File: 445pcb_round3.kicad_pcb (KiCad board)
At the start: 2 copper layers, 40 parts, among them J1 LED, J10 AVR-ISP-6, J2 LED, J3 LED, J4 SG3, J5 SG4, J6 SG5, J7 SG6, J8 SG1, J9 SG2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

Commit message: Add files via upload
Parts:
- added J11: SG1, Connector_Molex:Molex_KK-254_AE-6410-02A_1x02_P2.54mm_Vertical, F.Cu at (81.3, 76.2)
- added J13: LED, Connector_Molex:Molex_KK-254_AE-6410-02A_1x02_P2.54mm_Vertical, F.Cu at (81.3, 68.6)
- added P1: USB_C_Plug_USB2.0, Connector_USB:USB_C_Plug_Molex_105444, F.Cu at (78.7, 58.7)
- added R25: 1k, Resistor_SMD:R_0805_2012Metric_Pad1.20x1.40mm_HandSolder, F.Cu at (90.4, 73.7)
- added SW1: SW_SPST, Button_Switch_THT:SW_DIP_SPSTx01_Slide_9.78x4.72mm_W7.62mm_P2.54mm, F.Cu at (90.2, 80.5)
- moved R11 9.16 mm to (138.2, 61.0)
- moved R19 8.89 mm to (86.4, 48.3), turned to 90 degrees
- turned R8 to 180 degrees
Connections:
- R3 pad 1: Net-(U3-PD0) -> Net-(U3-PD3)
- U3 pad 1: unconnected-(U3-PD3-Pad1) -> Net-(U3-PD3)
- U3 pad 30: Net-(U3-PD0) -> UART RXD
- U3 pad 31: unconnected-(U3-PD1-Pad31) -> UART TXD
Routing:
- net Net-(U3-PD3): track 0.00 -> 134.4 mm, vias 0 -> 2
- net Net-(U3-PD0): track 118.4 -> 0.00 mm
- net Vdiff1: track 19.0 -> 98.8 mm, vias 0 -> 2
- net GND: track 360.4 -> 431.7 mm, vias 0 -> 2
- net +5V: track 269.5 -> 322.4 mm, vias 0 -> 5
- net Net-(U1-REGOUT): track 0.00 -> 24.3 mm, vias 0 -> 1
- net UART RXD: track 0.00 -> 21.3 mm, vias 0 -> 1
- net UART TXD: track 0.00 -> 19.9 mm, vias 0 -> 1
- net Net-(J11-Pin_2): track 0.00 -> 17.9 mm
- net MCU_DL: track 0.00 -> 17.0 mm, vias 0 -> 2
- net Net-(U5A--): track 13.2 -> 28.6 mm, vias 0 -> 2
- net unconnected-(P1-SHIELD-PadS1): track 0.00 -> 14.2 mm, vias 0 -> 1
- net Net-(J11-Pin_1): track 0.00 -> 10.7 mm
- net Net-(U4A-+): track 7.84 -> 15.8 mm, vias 0 -> 1
- net RST: track 32.0 -> 24.3 mm
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
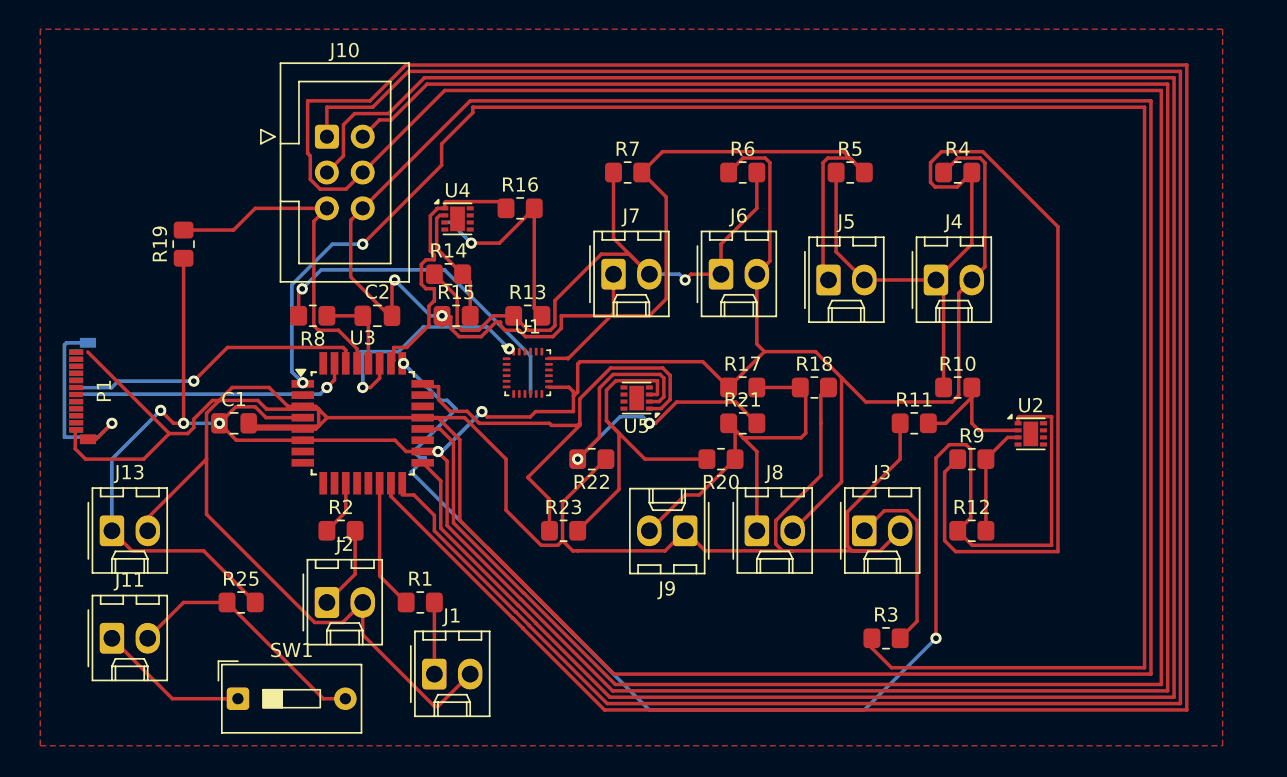
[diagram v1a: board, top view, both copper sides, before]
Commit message: adding power to op-amps, switching USB to connector, zener diode
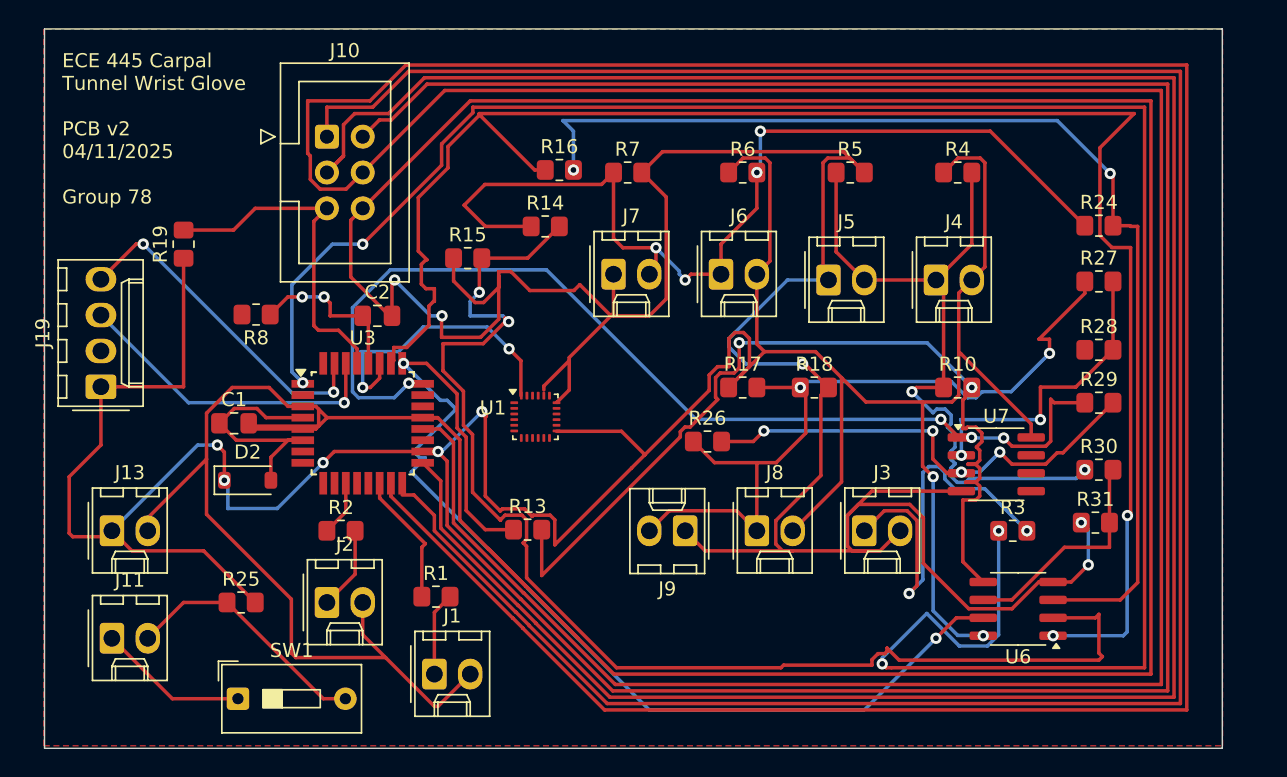
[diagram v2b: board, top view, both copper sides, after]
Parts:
- removed P1: USB_C_Plug_USB2.0, Connector_USB:USB_C_Plug_Molex_105444
- removed R11, R12, R22, R23: 3.3M, Resistor_SMD:R_0805_2012Metric_Pad1.20x1.40mm_HandSolder
- removed R20, R21, R9: 10k, Resistor_SMD:R_0805_2012Metric_Pad1.20x1.40mm_HandSolder
- removed U2, U4, U5: LM358_DFN, Package_DFN_QFN:DFN-8-1EP_2x2mm_P0.5mm_EP1.05x1.75mm
- added D2: MBR0520, Diode_SMD:D_SOD-123, F.Cu at (90.9, 65.0)
- added J19: Conn_01x04_Pin, Connector_Molex:Molex_KK-254_AE-6410-04A_1x04_P2.54mm_Vertical, F.Cu at (80.5, 58.4)
- added R24: 10k, Resistor_SMD:R_0805_2012Metric_Pad1.20x1.40mm_HandSolder, F.Cu at (151.2, 47.0)
- added R26: 10k, Resistor_SMD:R_0805_2012Metric_Pad1.20x1.40mm_HandSolder, F.Cu at (123.5, 62.2)
- added R27: 10k, Resistor_SMD:R_0805_2012Metric_Pad1.20x1.40mm_HandSolder, F.Cu at (151.2, 50.9)
- added R28: 3.3M, Resistor_SMD:R_0805_2012Metric_Pad1.20x1.40mm_HandSolder, F.Cu at (151.2, 55.8)
- added R29: 3.3M, Resistor_SMD:R_0805_2012Metric_Pad1.20x1.40mm_HandSolder, F.Cu at (151.2, 59.5)
- added R30: 10k, Resistor_SMD:R_0805_2012Metric_Pad1.20x1.40mm_HandSolder, F.Cu at (151.2, 64.2)
- added R31: 3.3M, Resistor_SMD:R_0805_2012Metric_Pad1.20x1.40mm_HandSolder, F.Cu at (151.0, 68.0)
- added U6: LM358DT, Package_SO:SOIC-8_3.9x4.9mm_P1.27mm, F.Cu at (145.5, 74.1)
- added U7: LM358DT, Package_SO:SOIC-8_3.9x4.9mm_P1.27mm, F.Cu at (144.0, 63.9)
- R13: value 10k -> 3.3M
- moved R13 15.2 mm to (110.8, 68.5)
- moved R3 11.8 mm to (145.1, 68.6)
- moved R14 7.65 mm to (112.0, 47.0)
- moved R15 4.17 mm to (106.5, 49.2)
- moved R8 4.02 mm to (91.5, 53.2)
- moved R16 3.89 mm to (113.0, 43.0)
- moved U1 3.17 mm to (111.3, 60.5)
- moved R1 1.18 mm to (104.2, 73.2)
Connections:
- C1 pad 1: +5V -> Net-(D2-A)
- R10 pad 2: Net-(U2A--) -> Net-(U6-IN2+)
- R13 pad 1: V2+ -> Vdiff1
- R13 pad 2: Net-(U4A-+) -> Net-(U6-IN2+)
- R16 pad 2: Net-(U4A-+) -> Net-(U6-IN1+)
- U1 pad 9: unconnected-(U1-SDO/AD0-Pad9) -> GND
- U3 pad 4: +5V -> Net-(D2-A)
- U3 pad 6: +5V -> Net-(D2-A)
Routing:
- net Vdiff2: track 20.1 -> 120.2 mm, vias 0 -> 2
- net Net-(U6-IN1-): track 8.55 -> 91.4 mm, vias 0 -> 2
- net Net-(U6-IN1+): track 0.00 -> 81.5 mm, vias 0 -> 2
- net Net-(U6-IN2+): track 0.00 -> 64.5 mm, vias 0 -> 2
- net +5V: track 322.4 -> 384.5 mm, vias 5 -> 7
- net Vdiff: track 35.5 -> 71.3 mm, vias 0 -> 4
- net Net-(U7-IN1+): track 0.00 -> 33.2 mm, vias 0 -> 4
- net V1+: track 84.0 -> 51.1 mm, vias 0 -> 2
- net Net-(U5A--): track 28.6 -> 0.00 mm, vias 2 -> 0
- net V+: track 30.9 -> 56.4 mm, vias 0 -> 2
- net Net-(U5A-+): track 25.2 -> 0.00 mm
- net V2+: track 44.7 -> 69.9 mm, vias 2 -> 4
- net Net-(U1-REGOUT): track 24.3 -> 0.00 mm, vias 1 -> 0
- net Net-(U7-IN1-): track 0.00 -> 21.6 mm, vias 0 -> 2
- net Vdiff1: track 98.8 -> 79.1 mm
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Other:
- board outline added: 83.5 x 51 mm
- board text added: "ECE 445 Carpal Tunnel Wrist Glove PCB v2 04/11/2025 Group 78"

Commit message: Add files via upload
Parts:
- moved U7 25.7 mm to (119.3, 71.1)
- moved U6 16.2 mm to (129.6, 71.1)
- moved R30 14.1 mm to (137.5, 67.3)
- moved SW1 13.8 mm to (103.5, 76.8)
- moved R31 13.8 mm to (137.4, 70.5)
- moved R24 12.9 mm to (139.4, 52.1)
- moved R27 12.8 mm to (139.4, 55.9)
- moved R29 12.5 mm to (139.4, 63.5)
- moved R28 12.5 mm to (139.4, 59.7)
- moved R17 10.3 mm to (115.8, 56.5)
- moved R10 10.2 mm to (131.2, 56.5)
- moved R3 8.90 mm to (137.4, 73.0)
- moved R4 8.16 mm to (133.1, 43.2)
- moved J2 8.04 mm to (88.9, 76.2)
- moved J1 8.03 mm to (96.5, 76.2)
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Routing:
- net MOSI: track 347.2 -> 150.8 mm, vias 0 -> 1
- net GND: track 434.7 -> 246.0 mm, vias 5 -> 9
- net +5V: track 384.5 -> 300.1 mm, vias 7 -> 8
- net Net-(J11-Pin_2): track 17.9 -> 60.0 mm
- net Vdiff1: track 79.1 -> 42.0 mm, vias 2 -> 3
- net Net-(U3-PD3): track 151.1 -> 118.6 mm, vias 4 -> 2
- net Net-(U6-IN2+): track 64.5 -> 33.0 mm, vias 2 -> 0
- net Net-(U6-IN1+): track 81.5 -> 111.6 mm, vias 2 -> 3
- net Net-(U6-IN1-): track 91.4 -> 63.7 mm, vias 2 -> 0
- net Net-(U7-IN1+): track 33.2 -> 58.5 mm, vias 4 -> 3
- net Net-(J11-Pin_1): track 10.7 -> 30.5 mm
- net MISO: track 170.4 -> 151.6 mm
- net SCK: track 171.8 -> 153.3 mm
- net V+: track 56.4 -> 38.7 mm
- net IMU_OUT: track 11.6 -> 25.6 mm
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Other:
- board size 83.5 x 51 mm -> 73.3 x 51 mm

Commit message: Add files via upload
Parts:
- removed D2: MBR0520, Diode_SMD:D_SOD-123
- added D3: MBR0520, Diode_SMD:D_SOD-123, F.Cu at (90.5, 64.8)
- moved U1 1.22 mm to (111.3, 59.3)
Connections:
- C1 pad 1: Net-(D2-A) -> +5V
- J10 pad 2: +5V -> Net-(D3-A)
- U3 pad 4: Net-(D2-A) -> +5V
- U3 pad 6: Net-(D2-A) -> +5V
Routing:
- net +5V: track 300.1 -> 167.9 mm
- net GND: track 246.0 -> 342.3 mm, vias 9 -> 16
- net Net-(D3-A): track 0.00 -> 62.7 mm, vias 0 -> 1
- net Net-(D2-A): track 12.6 -> 0.00 mm
- net MCU_DL: track 21.2 -> 20.0 mm
- net MOSI: vias 1 -> 2

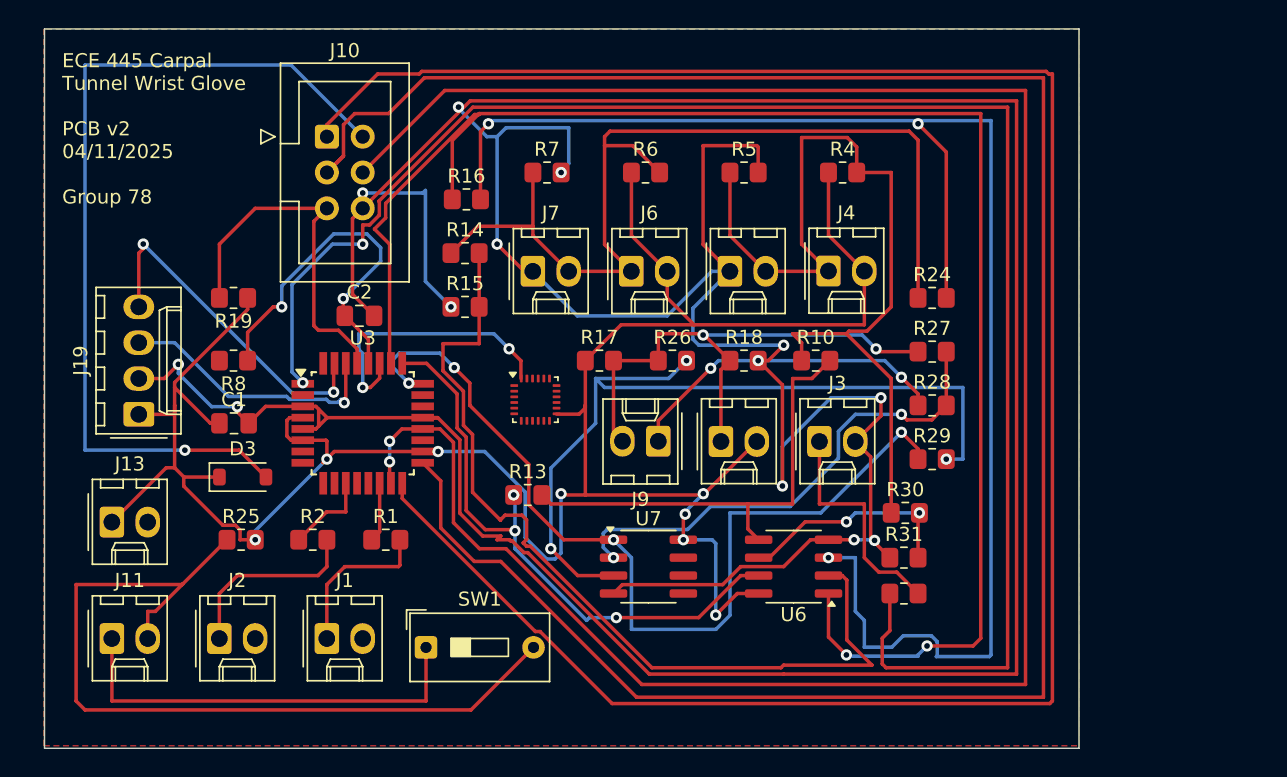
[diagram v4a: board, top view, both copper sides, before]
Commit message: IMU connections for new PCB
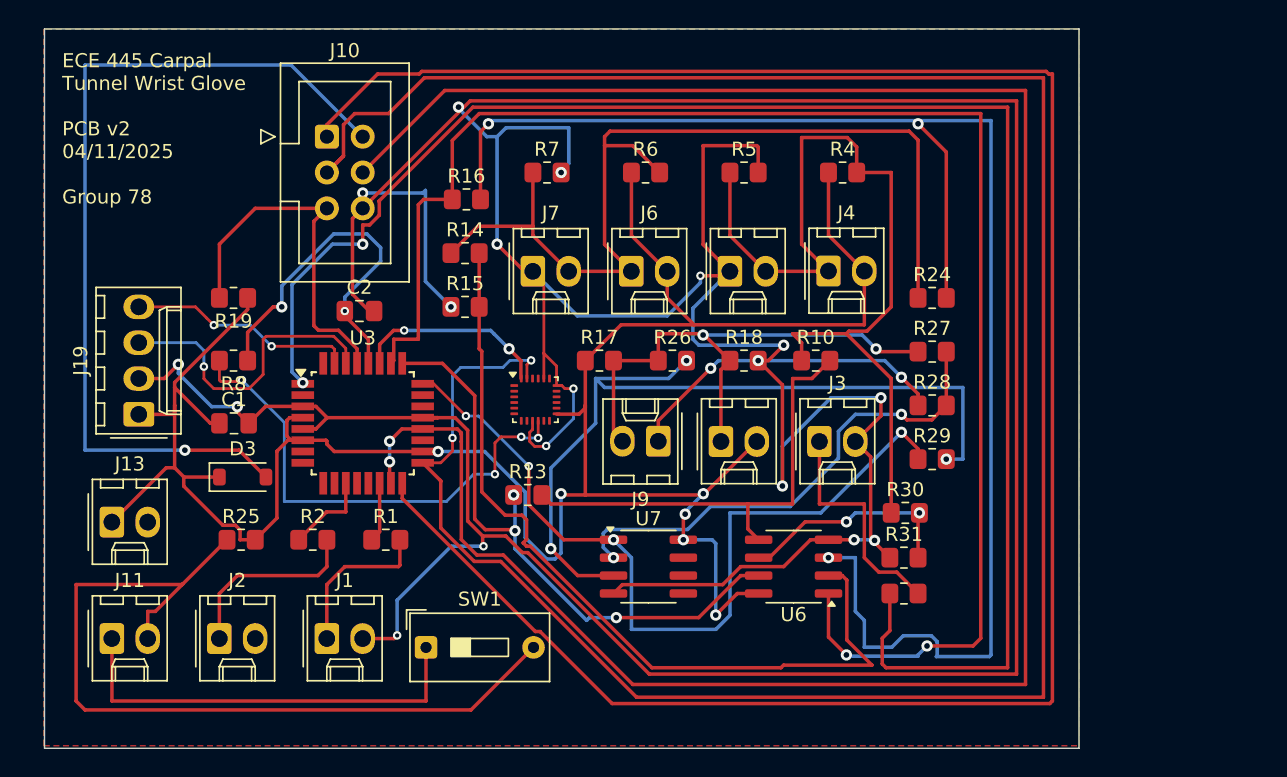
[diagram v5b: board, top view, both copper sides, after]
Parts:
- moved C2 0.34 mm to (98.8, 53.0)
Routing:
- net Net-(U1-REGOUT): track 0.00 -> 35.4 mm, vias 0 -> 4
- net GND: track 342.3 -> 374.7 mm, vias 16 -> 20
- net SCK: track 153.3 -> 168.6 mm, vias 0 -> 2
- net UART TXD: track 24.6 -> 16.2 mm
- net Vdiff: track 64.5 -> 58.3 mm
- net MCU_DL: track 20.0 -> 13.9 mm
- net Vdiff2: track 116.1 -> 110.3 mm
- net Net-(U6-IN1-): track 63.7 -> 59.4 mm
- net UART RXD: track 19.3 -> 22.4 mm
- net MOSI: track 150.8 -> 151.9 mm
- net Vdiff1: track 42.0 -> 42.6 mm
- net +5V: track 167.9 -> 167.3 mm, vias 8 -> 6
